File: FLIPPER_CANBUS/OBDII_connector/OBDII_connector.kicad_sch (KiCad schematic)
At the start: 2 parts, among them J1 Conn_02x08_Counter_Clockwise, J2 Conn_01x02

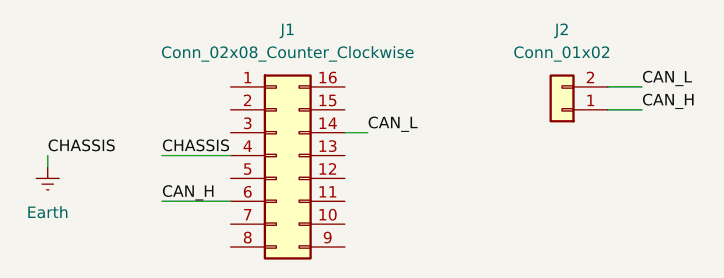
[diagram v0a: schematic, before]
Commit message: feat: information about OBDII got updated
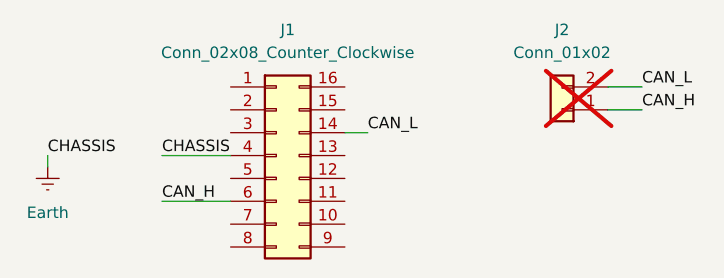
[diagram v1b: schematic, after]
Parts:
- J1: #MANUF (none) -> 20240401-1008-1; PROVEEDOR (none) -> UNIT
- J2: now not fitted
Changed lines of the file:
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@@
 		(in_bom yes)
 		(on_board yes)
-		(dnp no)
+		(dnp yes)
 		(fields_autoplaced yes)
 		(property "Reference" "J2"
@@
 		)
 		(property "Description" "Generic connector, single row, 01x02, script generated (kicad-library-utils/schlib/autogen/connector/)"
+			(at 87.63 34.29 0)
+			(effects
+				(font
+					(size 1.27 1.27)
+				)
+				(hide yes)
+			)
+		)
+		(property "#MANUF" ""
+			(at 87.63 34.29 0)
+			(effects
+				(font
+					(size 1.27 1.27)
+				)
+				(hide yes)
+			)
+		)
+		(property "PROVEEDOR" ""
 			(at 87.63 34.29 0)
 			(effects
@@
 			)
 		)
-		(property "Datasheet" "~"
+		(property "Datasheet" "https://www.flexihub.com/images/upload/flexihub/articles/diagnostics/pinout_explanation.jpg"
 			(at 55.88 39.37 0)
 			(effects
@@
 			(at 55.88 39.37 0)
 			(effects
+				(font
+					(size 1.27 1.27)
+				)
+				(hide yes)
+			)
+		)
+		(property "#MANUF" "20240401-1008-1"
+			(at 55.88 39.37 0)
+			(effects
+				(font
+					(size 1.27 1.27)
+				)
+				(hide yes)
+			)
+		)
+		(property "PROVEEDOR" "UNIT"
+			(at 55.88 39.37 0)
+			(effects

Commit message: feat: change shape of PCB & indicators added
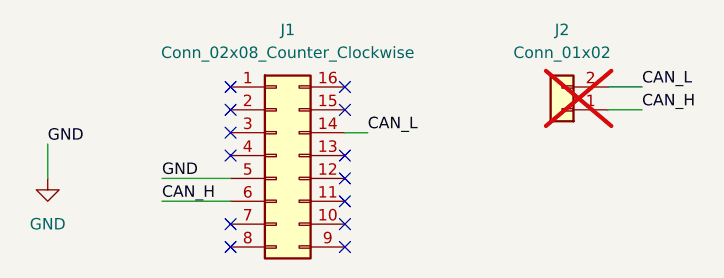
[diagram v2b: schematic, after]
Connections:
- net GND: now reaches J1.5 (Pin_5)
- net Earth: no longer names the net of J1.4 (Pin_4)
- no-connect marks 0 -> 13
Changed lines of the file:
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@@
 	(generator_version "8.0")
 	(paper "A4")
+	(no_connect
+		(at 50.8 31.75)
+	)
+	(no_connect
+		(at 50.8 36.83)
+	)
+	(no_connect
+		(at 50.8 49.53)
+	)
+	(no_connect
+		(at 63.5 44.45)
+	)
+	(no_connect
+		(at 63.5 41.91)
+	)
+	(no_connect
+		(at 63.5 46.99)
+	)
+	(no_connect
+		(at 63.5 31.75)
+	)
+	(no_connect
+		(at 63.5 49.53)
+	)
+	(no_connect
+		(at 50.8 39.37)
+	)
+	(no_connect
+		(at 50.8 46.99)
+	)
+	(no_connect
+		(at 50.8 34.29)
+	)
+	(no_connect
+		(at 63.5 39.37)
+	)
+	(no_connect
+		(at 63.5 34.29)
+	)
 	(wire
 		(pts
@@
 	(wire
 		(pts
-			(xy 30.48 39.37) (xy 30.48 40.64)
-		)
-		(stroke
-			(width 0)
-			(type default)
-		)
-	)
-	(wire
-		(pts
-			(xy 43.18 39.37) (xy 50.8 39.37)
+			(xy 43.18 41.91) (xy 50.8 41.91)
+		)
+		(stroke
+			(width 0)
+			(type default)
+		)
+	)
+	(wire
+		(pts
+			(xy 30.48 38.1) (xy 30.48 41.91)
 		)
 		(stroke
@@
 		)
 	)
-	(label "CHASSIS"
-		(at 43.18 39.37 0)
-		(fields_autoplaced yes)
-		(effects
-			(font
-				(size 1.27 1.27)
-			)
-			(justify left bottom)
-		)
-	)
 	(label "CAN_H"
 		(at 43.18 44.45 0)
@@
 		)
 	)
-	(label "CHASSIS"
-		(at 30.48 39.37 0)
-		(fields_autoplaced yes)
-		(effects
-			(font
-				(size 1.27 1.27)
-			)
-			(justify left bottom)
+	(label "GND"
+		(at 30.48 38.1 0)
+		(fields_autoplaced yes)
+		(effects
+			(font
+				(size 1.27 1.27)
+			)
+			(justify left bottom)
+		)
+	)
+	(label "GND"
+		(at 43.18 41.91 0)
+		(fields_autoplaced yes)
+		(effects
+			(font
+				(size 1.27 1.27)
+			)
+			(justify left bottom)
+		)
+	)
+	(symbol
+		(lib_id "power:GND")
+		(at 30.48 41.91 0)
+		(unit 1)
+		(exclude_from_sim no)
+		(in_bom yes)
+		(on_board yes)
+		(dnp no)
+		(fields_autoplaced yes)
+		(property "Reference" "#PWR01"
+			(at 30.48 48.26 0)
+			(effects
+				(font
+					(size 1.27 1.27)
+				)
+				(hide yes)
+			)
+		)
+		(property "Value" "GND"
+			(at 30.48 46.99 0)
+			(effects
+				(font
+					(size 1.27 1.27)
+				)
+			)
+		)
+		(property "Footprint" ""
+			(at 30.48 41.91 0)
+			(effects
+				(font
+					(size 1.27 1.27)
+				)
+				(hide yes)
+			)
+		)
+		(property "Datasheet" ""
+			(at 30.48 41.91 0)
+			(effects
+				(font
+					(size 1.27 1.27)
+				)
+				(hide yes)
+			)
+		)
+		(property "Description" "Power symbol creates a global label with name \"GND\" , ground"
+			(at 30.48 41.91 0)
+			(effects
+				(font
+					(size 1.27 1.27)
+				)
+				(hide yes)
+			)
+		)
+		(pin "1"
+		)
+		(instances
+			(project "OBDII_connector"
+				(path "/0a2cdc7f-9f05-4234-abf0-4d9ef4a14a4e"
+					(reference "#PWR01")
+					(unit 1)
+				)
+			)
 		)
 	)
@@
 					(unit 1)
 				)
-			)
-		)
-	)
-	(symbol
-		(lib_id "power:Earth")
-		(at 30.48 40.64 0)
-		(unit 1)
-		(exclude_from_sim no)
-		(in_bom yes)
-		(on_board yes)
-		(dnp no)
-		(fields_autoplaced yes)
-		(property "Reference" "#PWR01"
-			(at 30.48 46.99 0)
-			(effects
-				(font
-					(size 1.27 1.27)
-				)
-				(hide yes)
-			)
-		)
-		(property "Value" "Earth"
-			(at 30.48 45.72 0)
-			(effects
-				(font
-					(size 1.27 1.27)
-				)
-			)
-		)
-		(property "Footprint" ""
-			(at 30.48 40.64 0)
-			(effects
-				(font
-					(size 1.27 1.27)
-				)
-				(hide yes)
-			)
-		)
-		(property "Datasheet" "~"
-			(at 30.48 40.64 0)
-			(effects
-				(font
-					(size 1.27 1.27)
-				)
-				(hide yes)
-			)
-		)
-		(property "Description" "Power symbol creates a global label with name \"Earth\""
-			(at 30.48 40.64 0)
-			(effects
-				(font
-					(size 1.27 1.27)
-				)
-				(hide yes)
-			)
-		)
-		(pin "1"
-		)
-		(instances
-			(project "OBDII_connector"
-				(path "/0a2cdc7f-9f05-4234-abf0-4d9ef4a14a4e"
-					(reference "#PWR01")
-					(unit 1)
-				)

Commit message: feat: new dimensions added for OBDII connector
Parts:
- J1: footprint Case:OBD-II-Sparkfun -> Case:OBD-II-Sparkfun v2.0
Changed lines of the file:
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@@
 			)
 		)
-		(property "Footprint" "Case:OBD-II-Sparkfun"
+		(property "Footprint" "Case:OBD-II-Sparkfun v2.0"
 			(at 55.88 39.37 0)
 			(effects
